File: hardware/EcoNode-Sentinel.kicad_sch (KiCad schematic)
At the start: 0 parts

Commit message: hardware: complete Day 3 schematic design for PDN and ESP32 power rails
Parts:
- added J1: USB_C_Receptacle_USB2.0_16P, symbol Connector:USB_C_Receptacle_USB2.0_16P
- added U1: AP2112K-3.3, Package_TO_SOT_SMD:SOT-23-5, symbol Regulator_Linear:AP2112K-3.3
- added U2: ESP32-S3-WROOM-1, RF_Module:ESP32-S3-WROOM-1, symbol RF_Module:ESP32-S3-WROOM-1
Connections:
- new net: J1.A1 (GND), J1.A12 (GND), J1.B1 (GND), J1.B12 (GND)
- new net: J1.A4 (VBUS), J1.A9 (VBUS), J1.B4 (VBUS), J1.B9 (VBUS)
- new net: U2.1 (GND), U2.40 (GND), U2.41 (GND)

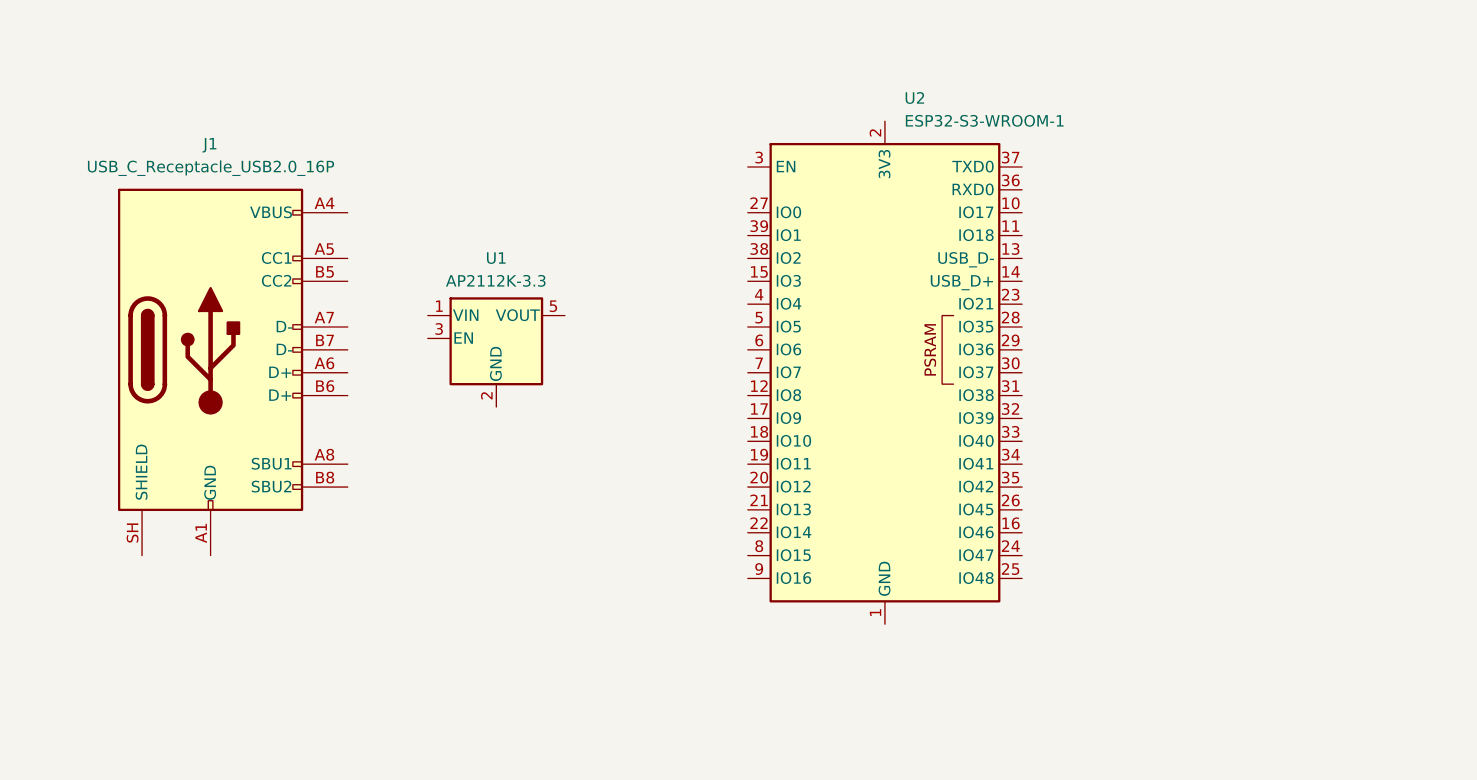
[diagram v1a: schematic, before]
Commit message: hardware: configure 4-layer stackup matrix, power net classes, and floorplan day 4
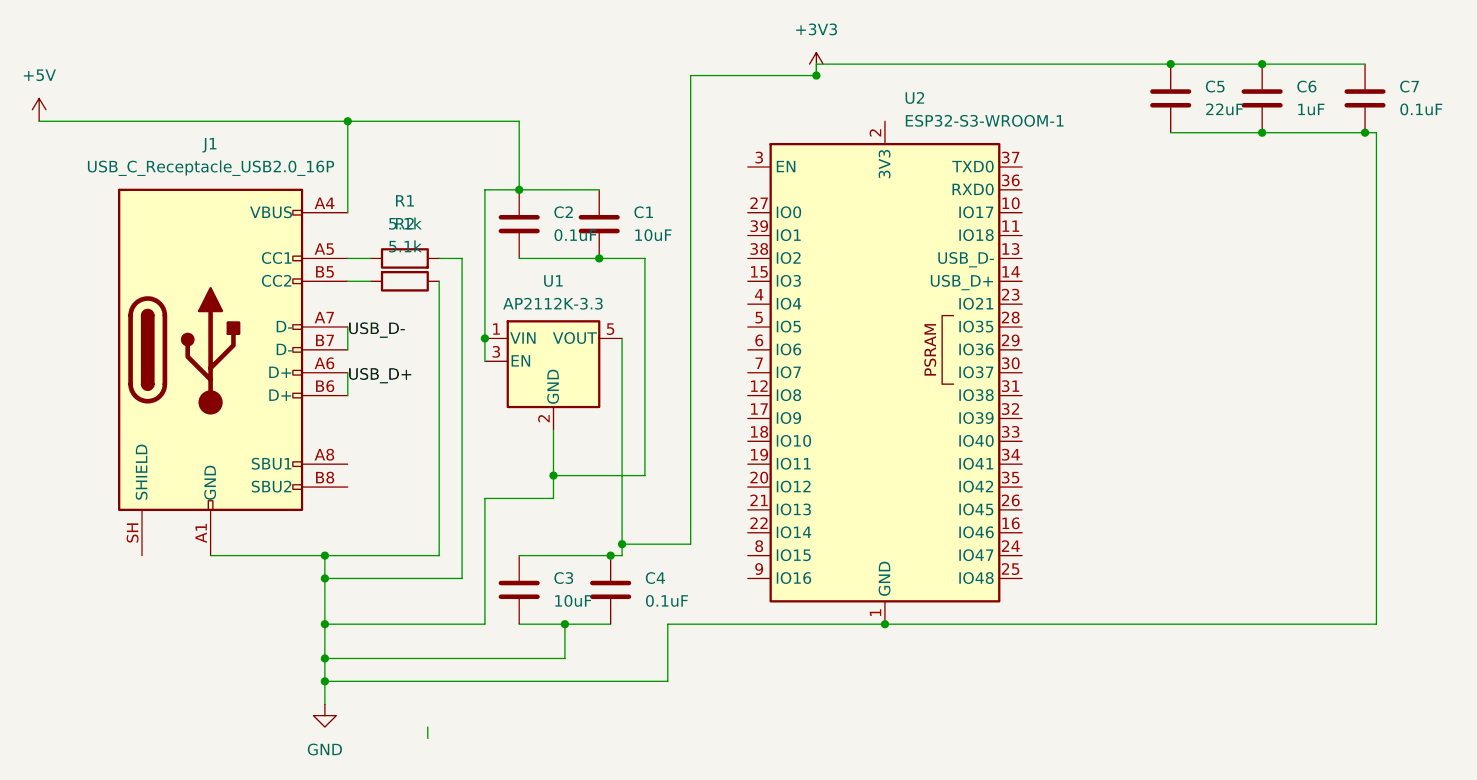
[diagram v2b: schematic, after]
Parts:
- added C1, C3: 10uF, Capacitor_SMD:C_0805_2012Metric, symbol Device:C
- added C2, C4, C7: 0.1uF, Capacitor_SMD:C_0603_1608Metric, symbol Device:C
- added C5: 22uF, Capacitor_SMD:C_1206_3216Metric, symbol Device:C
- added C6: 1uF, Capacitor_SMD:C_0603_1608Metric, symbol Device:C
- added R1, R2: 5.1k, Resistor_SMD:R_0603_1608Metric, symbol Device:R
- J1: footprint (none) -> Connector_USB:USB_C_Receptacle_GCT_USB4105-xx-A_16P_TopMnt_Horizontal
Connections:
- net GND: now reaches J1.A1 (GND), J1.A12 (GND), J1.B1 (GND), J1.B12 (GND)
- net GND: now also U1.2 (GND), U2.1 (GND), U2.40 (GND), U2.41 (GND), C1.1, C2.2, C3.2, C4.2, C5.2, C6.2, C7.2, R1.2, R2.1
- net +5V: now reaches J1.A4 (VBUS), J1.A9 (VBUS), J1.B4 (VBUS), J1.B9 (VBUS)
- net +5V: now also U1.1 (VIN), U1.3 (EN), C1.2, C2.1
- net at J1.A5 (CC1): now also R1.1
- net  USB_D+: now reaches J1.A6 (D+)
- net  USB_D+: now also J1.B6 (D+)
- net USB_D-: now reaches J1.A7 (D-)
- net USB_D-: now also J1.B7 (D-)
- net at J1.B5 (CC2): now also R2.2
- net +3V3: now reaches U1.5 (VOUT)
- net +3V3: now also C3.1, C4.1, C5.1, C6.1, C7.1
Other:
- moved on the sheet: U1

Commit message: hardware: layout complete, zero DRC violations, paths verified in 3D
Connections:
- net  USB_D+ is gone; now on net USB_D+: J1.A6 (D+), J1.B6 (D+)
- net +3V3: now also U2.2 (3V3)
- net USB_D-: now also U2.13 (USB_D-)
- net USB_D+: now reaches U2.14 (USB_D+)
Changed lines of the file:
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@@
+	)
+	(junction
+		(at 199.39 69.85)
+		(diameter 0)
+		(color 0 0 0 0)
 	)
 	(junction
@@
 	(wire
 		(pts
-			(xy 231.14 69.85) (xy 191.77 69.85)
+			(xy 231.14 69.85) (xy 199.39 69.85)
 		)
 		(stroke
@@
 	(wire
 		(pts
+			(xy 139.7 104.14) (xy 139.7 106.68)
+		)
+		(stroke
+			(width 0)
+			(type default)
+		)
+	)
+	(wire
+		(pts
 			(xy 199.39 132.08) (xy 175.26 132.08)
 		)
@@
 	(wire
 		(pts
+			(xy 199.39 69.85) (xy 199.39 76.2)
+		)
+		(stroke
+			(width 0)
+			(type default)
+		)
+	)
+	(wire
+		(pts
 			(xy 172.72 91.44) (xy 172.72 115.57)
 		)
@@
 	(wire
 		(pts
+			(xy 199.39 69.85) (xy 191.77 69.85)
+		)
+		(stroke
+			(width 0)
+			(type default)
+		)
+	)
+	(wire
+		(pts
 			(xy 170.18 123.19) (xy 170.18 124.46)
 		)
@@
 	(wire
 		(pts
-			(xy 139.7 104.14) (xy 139.7 106.68)
-		)
-		(stroke
-			(width 0)
-			(type default)
-		)
-	)
-	(wire
-		(pts
 			(xy 172.72 115.57) (xy 162.56 115.57)
 		)
@@
 	(wire
 		(pts
-			(xy 148.59 143.51) (xy 148.59 144.78)
-		)
-		(stroke
-			(width 0)
-			(type default)
-		)
-	)
-	(wire
-		(pts
 			(xy 191.77 71.12) (xy 177.8 71.12)
 		)
@@
 		)
 	)
-	(label " USB_D+"
-		(at 139.7 105.41 0)
+	(label "USB_D-"
+		(at 139.7 100.33 0)
 		(effects
 			(font
@@
 		)
 	)
-	(label "USB_D-"
-		(at 139.7 100.33 0)
+	(label "USB_D+"
+		(at 214.63 93.98 0)
 		(effects
 			(font
+				(size 1.27 1.27)
+			)
+			(justify left bottom)
+		)
+	)
+	(label "USB_D-"
+		(at 214.63 91.44 0)
+		(effects
+			(font
+				(size 1.27 1.27)
+			)
+			(justify left bottom)
+		)
+	)
+	(label "USB_D+"
+		(at 139.7 106.68 0)
+		(effects
+			(font
